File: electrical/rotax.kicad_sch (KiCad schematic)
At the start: 23 parts

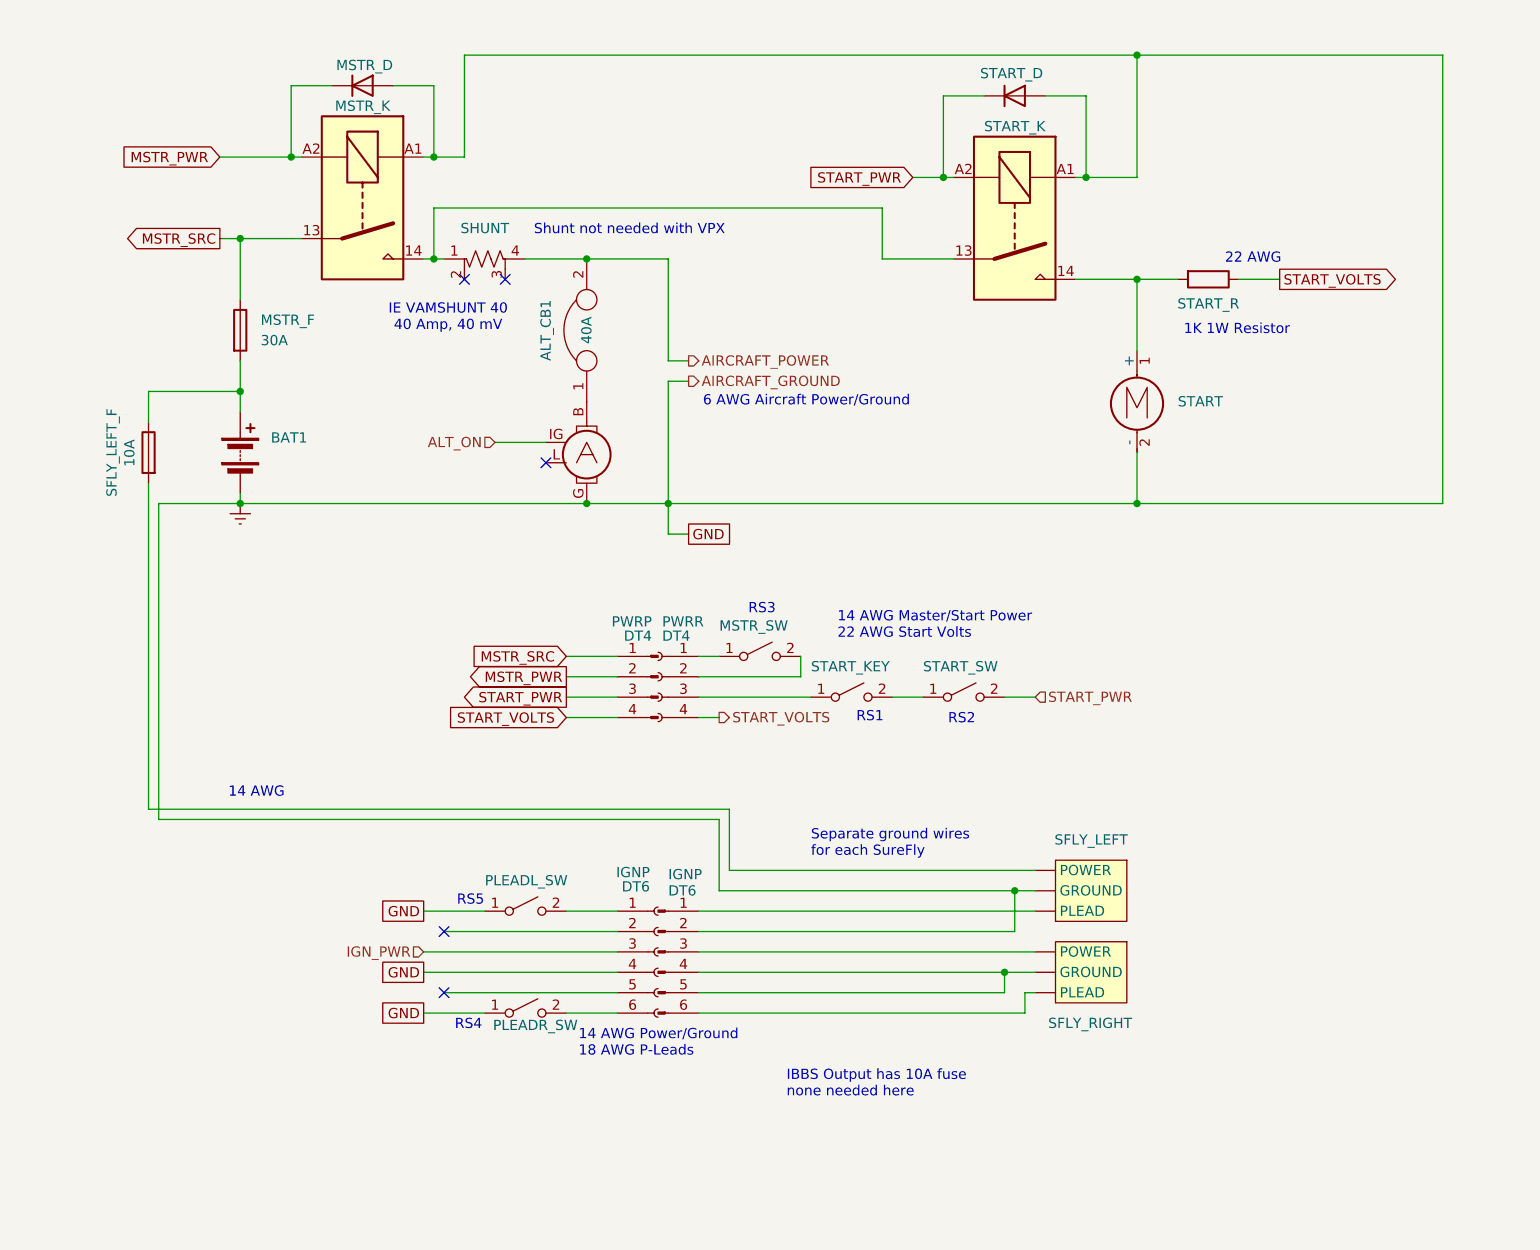
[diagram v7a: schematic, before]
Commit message: Switched over to using PPS instead of contactors.
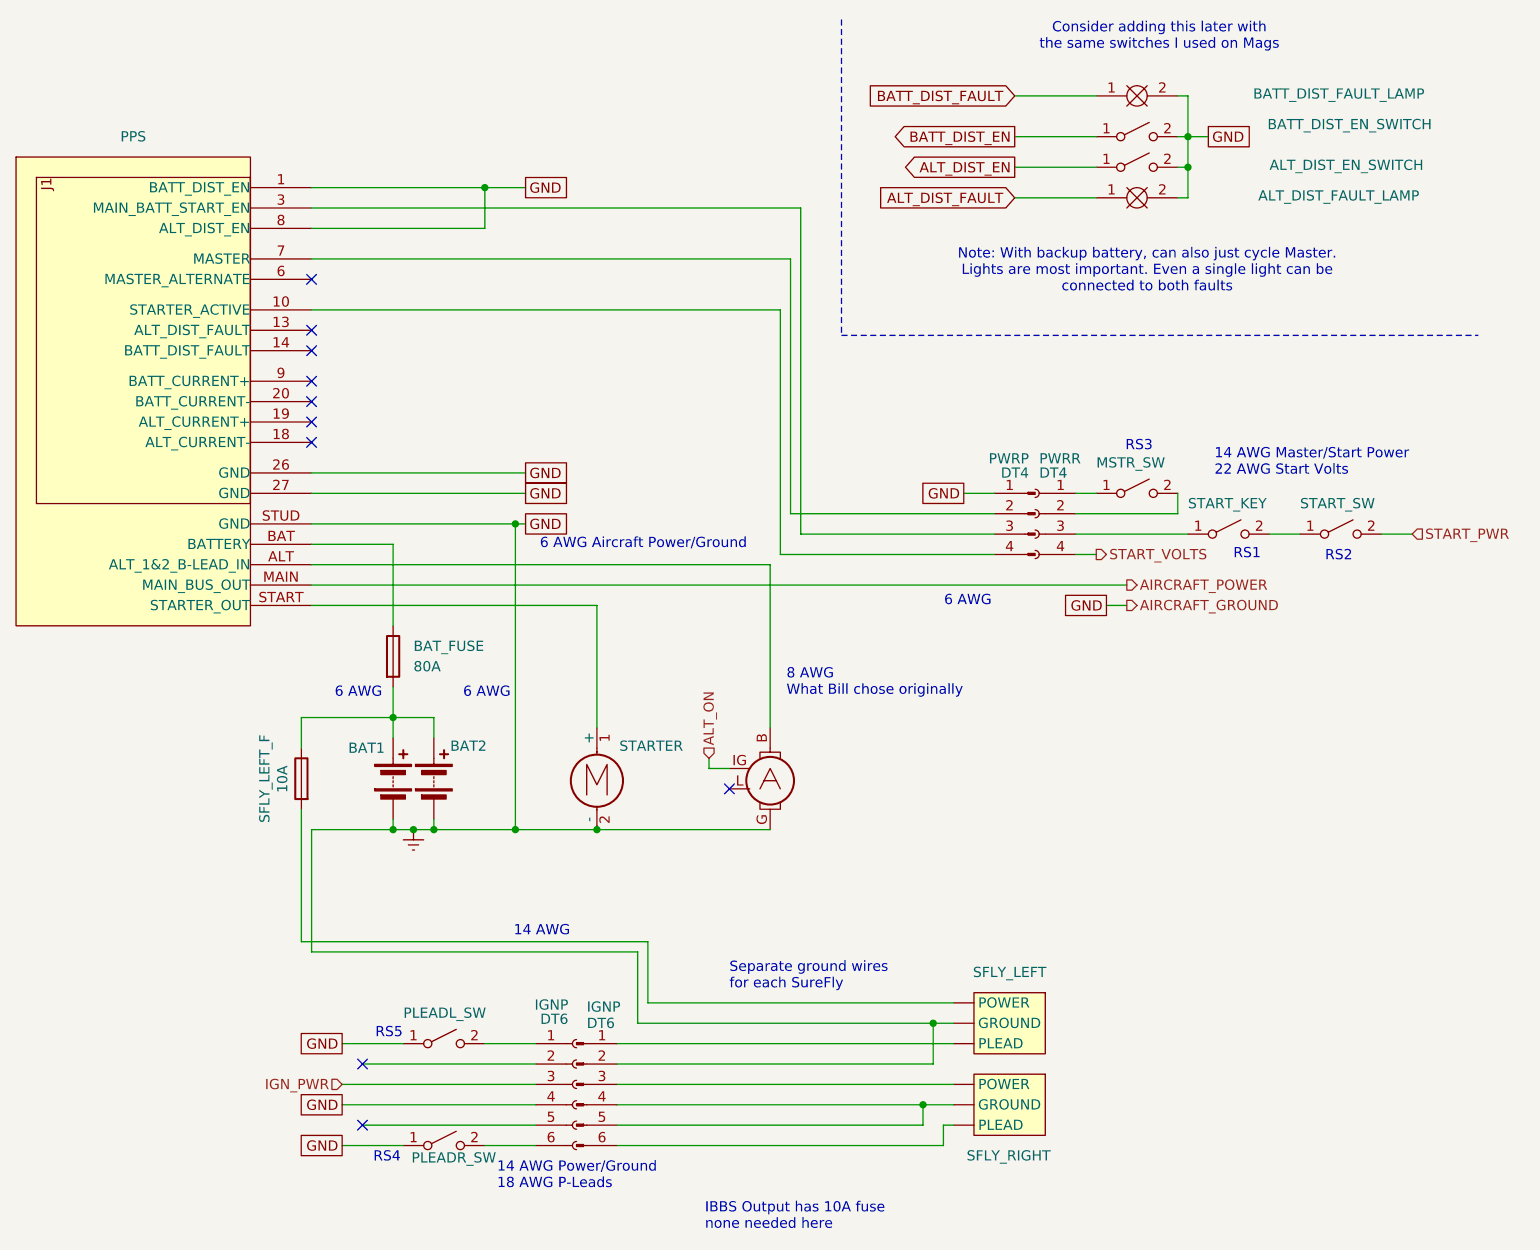
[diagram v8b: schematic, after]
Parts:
- removed ALT_CB1: 40A, symbol flyerx:Circuit_Breaker
- removed MSTR_D, START_D: 1N5400, Diode_THT:D_DO-201AD_P15.24mm_Horizontal, symbol Diode:1N5400
- removed MSTR_K, START_K: Fujitsu_FTR-LYAA005x, Relay_THT:Relay_SPST-NO_Fujitsu_FTR-LYAA005x_FormA_Vertical, symbol Relay:Fujitsu_FTR-LYAA005x
- removed SHUNT: R_Shunt_US, symbol Device:R_Shunt_US
- removed START_R: R, symbol Device:R
- added ALT_DIST_EN_SWITCH, BATT_DIST_EN_SWITCH: ~, symbol Switch:SW_SPST
- added ALT_DIST_FAULT_LAMP, BATT_DIST_FAULT_LAMP: ~, symbol flyerx:Bulb
- added BAT2: ~, symbol Device:Battery
- added PPS: ~, symbol flyerx:Vertical_Power_PPS
- BAT_FUSE: renamed from MSTR_F; value 30A -> 80A
- renumbered START to STARTER
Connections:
- net AIRCRAFT_POWER: now also PPS.MAIN (MAIN_BUS_OUT)
- net Earth: now also PWRP.1 (Pin_1), ALT_DIST_EN_SWITCH.2 (B), ALT_DIST_FAULT_LAMP.2, BAT2.2 (-), BATT_DIST_EN_SWITCH.2 (B), BATT_DIST_FAULT_LAMP.2, PPS.1 (BATT_DIST_EN), PPS.26 (GND), PPS.27 (GND), PPS.8 (ALT_DIST_EN), PPS.STUD (GND)
- net START_PWR: no longer PWRP.3 (Pin_3)
- net START_VOLTS: no longer PWRP.4 (Pin_4)
- net at STARTER.1 (+): now also PPS.START (STARTER_OUT)
- net at BAT1.1 (+), BAT_FUSE.2, SFLY_LEFT_F.1: now also BAT2.1 (+)
- net at A1.B: now also PPS.ALT (ALT_1&2_B-LEAD_IN)
- net MSTR_PWR: no longer names the net of PWRP.2 (Pin_2)
- net MSTR_PWR: now also PPS.7 (MASTER)
- net MSTR_SRC: no longer names the net of BAT_FUSE.1
- net MSTR_SRC: now also PPS.BAT (BATTERY); no longer PWRP.1 (Pin_1)
- new net: PPS.10 (STARTER_ACTIVE), PWRP.4 (Pin_4)
- new net: PPS.3 (MAIN_BATT_START_EN), PWRP.3 (Pin_3)
- new net ALT_DIST_EN: ALT_DIST_EN_SWITCH.1 (A)
- new net ALT_DIST_FAULT: ALT_DIST_FAULT_LAMP.1
- new net BATT_DIST_EN: BATT_DIST_EN_SWITCH.1 (A)
- new net BATT_DIST_FAULT: BATT_DIST_FAULT_LAMP.1
- no-connect marks 5 -> 10
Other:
- note added: "6 AWG"
- note added: "8 AWG What Bill chose originally"
- note added: "Consider adding this later with the same switches I used on Mags"
- note added: "Note: With backup battery, can also just cycle Master. Lights are most important. Even a single light can be connected to both faults"
- note removed: "1K 1W Resistor"
- note removed: "22 AWG"
- note removed: "IE VAMSHUNT 40 40 Amp, 40 mV"
- note removed: "Shunt not needed with VPX"
- moved on the sheet: BAT1, BAT_FUSE, IGNP, MSTR_SW, PLEADL_SW, PLEADR_SW, PWRP, PWRR, SFLY_LEFT, SFLY_LEFT_F, SFLY_RIGHT, STARTER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
